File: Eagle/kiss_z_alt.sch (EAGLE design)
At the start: 7 parts, among them U1 LMX2326, U2 MAX2752, U3 RMK-3-93+

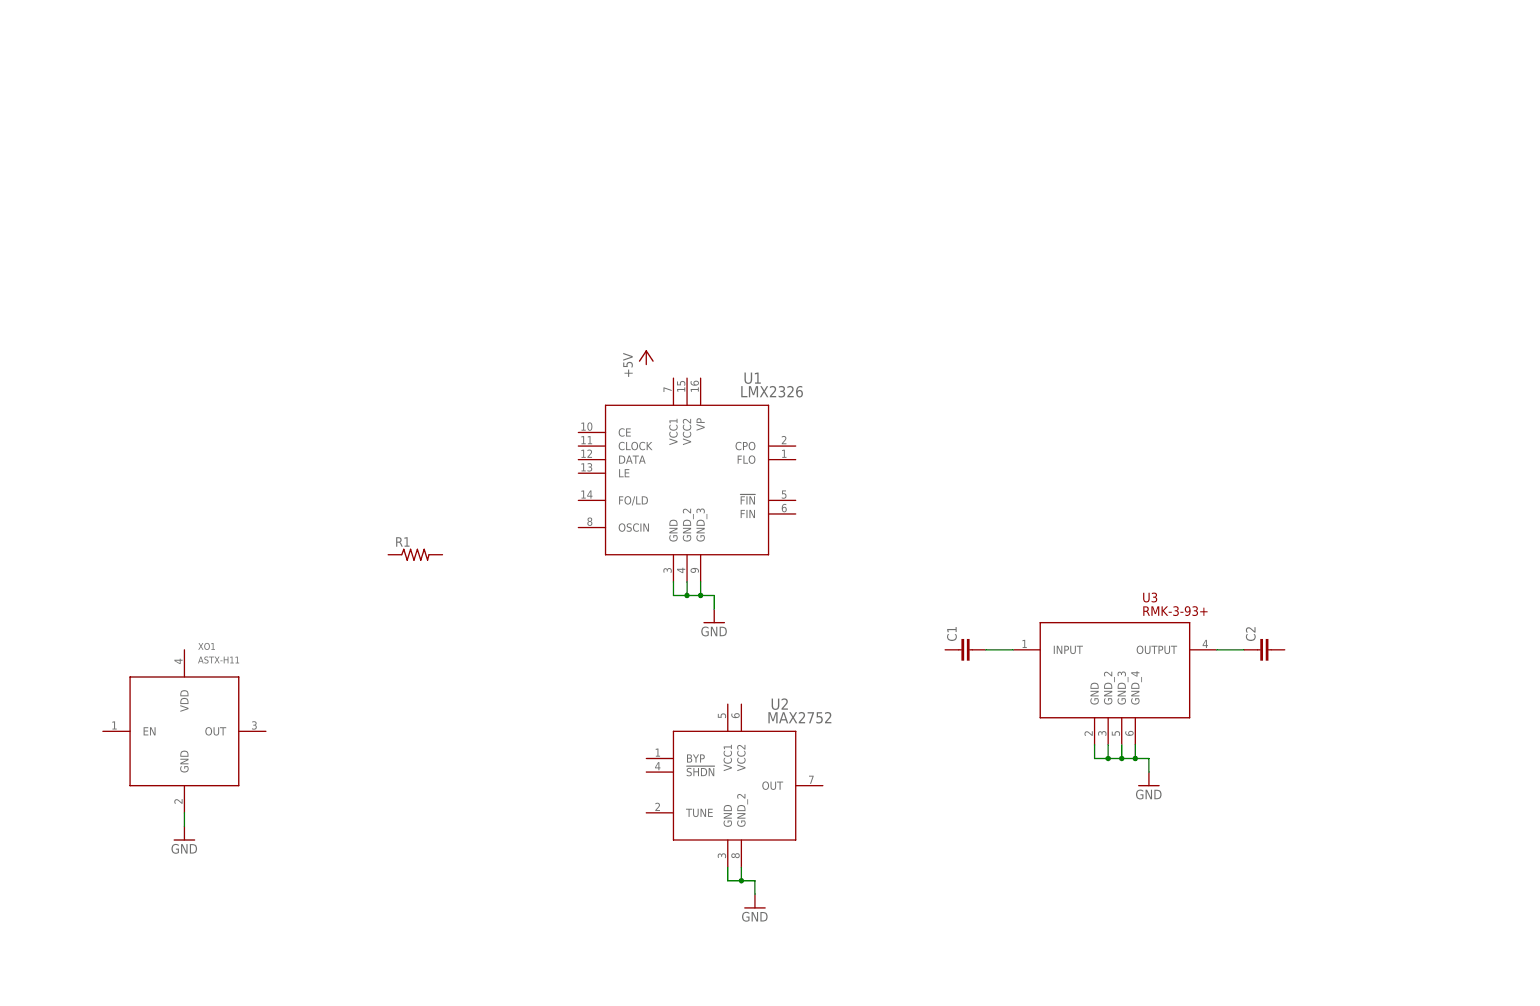
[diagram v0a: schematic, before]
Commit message: Making connections
made loop filter
started power connections
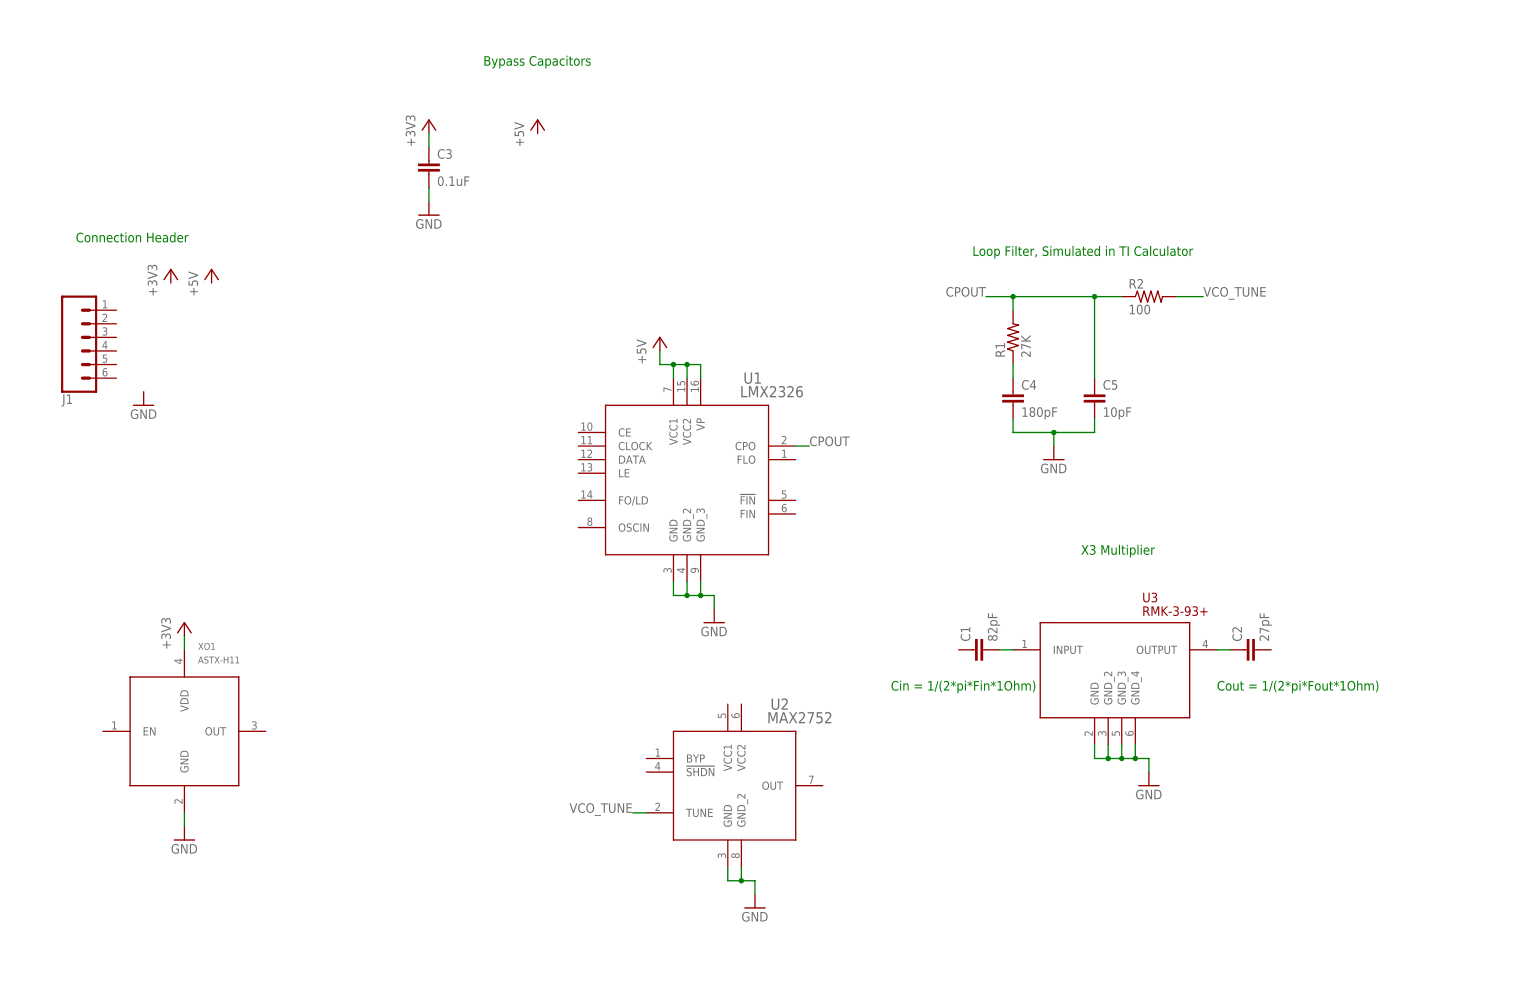
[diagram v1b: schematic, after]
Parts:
- added C3: 0.1uF, kiss_z:C0603
- added C4: 180pF, kiss_z:C0603
- added C5: 10pF, kiss_z:C0603
- added J1: (no value), SparkFun-Connectors:CONN_06SILK_FEMALE_PTH
- added R2: 100, kiss_z:R0603
- C1: value (none) -> 82pF
- C2: value (none) -> 27pF
- R1: value (none) -> 27K
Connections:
- new net +3V3: XO1.VDD
- new net +5V: U1.VCC1, U1.VCC2, U1.VP
- new net CPOUT: U1.CPO
- new net N$3: C4.1, R1.1
- new net N$4: U2.TUNE
- new net N$5: C5.1, R1.2, R2.1
- new net N$6: C3.1
- new net VCO_TUNE: R2.2
- net GND: now also C3.2, C4.2, C5.2
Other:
- note added: "Bypass Capacitors"
- note added: "Cin = 1/(2*pi*Fin*1Ohm)"
- note added: "Connection Header"
- note added: "Cout = 1/(2*pi*Fout*1Ohm)"
- note added: "Loop Filter, Simulated in TI Calculator"
- note added: "X3 Multiplier"
- moved on the sheet: C1, C2, R1

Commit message: more connections
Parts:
- added C6: NP, kiss_z:C0603
- added R3: NP, kiss_z:R0603
- C3: value 0.1uF -> 100pF
- C4: value 180pF -> 82pF
- C5: value 10pF -> 12pF
- R1: value 27K -> 56K
- R2: value 100 -> NP
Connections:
- removed net VCO_TUNE: R2.2
- new net FL_OUT: U1.FLO
- new net MULT_OUT: C2.2
- new net N$7: C6.2, R2.2, R3.1
- new net N$8: R3.2
- new net VCO_OUT: U2.OUT
- net +3V3: now also XO1.EN
- net GND: now also R2.1
- net N$5: now also C6.1; no longer R2.1
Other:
- note added: "VCO"
- moved on the sheet: R2
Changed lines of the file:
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@@
 <part name="XO1" library="kiss_z" deviceset="ASTX-H11" device=""/>
 <part name="U2" library="kiss_z" deviceset="MAX2752" device=""/>
-<part name="R1" library="kiss_z" deviceset="R0603" device="" value="27K"/>
+<part name="R1" library="kiss_z" deviceset="R0603" device="" value="56K"/>
 <part name="U3" library="kiss_z" deviceset="RMK-3-93+" device=""/>
 <part name="C1" library="kiss_z" deviceset="C0603" device="" value="82pF"/>
@@
 <part name="GND4" library="supply1" library_urn="urn:adsk.eagle:library:371" deviceset="GND" device=""/>
 <part name="+3V1" library="supply1" library_urn="urn:adsk.eagle:library:371" deviceset="+3V3" device=""/>
-<part name="C3" library="kiss_z" deviceset="C0603" device="" value="0.1uF"/>
+<part name="C3" library="kiss_z" deviceset="C0603" device="" value="100pF"/>
 <part name="GND5" library="supply1" library_urn="urn:adsk.eagle:library:371" deviceset="GND" device=""/>
-<part name="C4" library="kiss_z" deviceset="C0603" device="" value="180pF"/>
-<part name="C5" library="kiss_z" deviceset="C0603" device="" value="10pF"/>
+<part name="C4" library="kiss_z" deviceset="C0603" device="" value="82pF"/>
+<part name="C5" library="kiss_z" deviceset="C0603" device="" value="12pF"/>
 <part name="GND6" library="supply1" library_urn="urn:adsk.eagle:library:371" deviceset="GND" device=""/>
-<part name="R2" library="kiss_z" deviceset="R0603" device="" value="100"/>
 <part name="J1" library="SparkFun-Connectors" library_urn="urn:adsk.eagle:library:513" deviceset="CONN_06" device="SILK_FEMALE_PTH" package3d_urn="urn:adsk.eagle:package:38009/1"/>
 <part name="+3V2" library="supply1" library_urn="urn:adsk.eagle:library:371" deviceset="+3V3" device=""/>
@@
 <part name="+3V3" library="supply1" library_urn="urn:adsk.eagle:library:371" deviceset="+3V3" device=""/>
 <part name="P+3" library="supply1" library_urn="urn:adsk.eagle:library:371" deviceset="+5V" device=""/>
+<part name="R2" library="kiss_z" deviceset="R0603" device="" value="NP"/>
+<part name="R3" library="kiss_z" deviceset="R0603" device="" value="NP"/>
+<part name="C6" library="kiss_z" deviceset="C0603" device="" value="NP"/>
 </parts>
 <sheets>
@@
 <text x="165.1" y="53.34" size="1.778" layer="91">Cin = 1/(2*pi*Fin*1Ohm)</text>
 <text x="226.06" y="53.34" size="1.778" layer="91">Cout = 1/(2*pi*Fout*1Ohm)</text>
-<text x="180.34" y="134.62" size="1.778" layer="91">Loop Filter, Simulated in TI Calculator</text>
-<text x="200.66" y="78.74" size="1.778" layer="91">X3 Multiplier</text>
+<text x="193.04" y="134.62" size="1.778" layer="91">Loop Filter, Simulated in TI Calculator</text>
+<text x="200.66" y="73.66" size="1.778" layer="91">X3 Multiplier</text>
 <text x="12.7" y="137.16" size="1.778" layer="91">Connection Header</text>
 <text x="88.9" y="170.18" size="1.778" layer="91">Bypass Capacitors</text>
+<text x="76.2" y="162.56" size="1.778" layer="91">VCO</text>
 </plain>
 <instances>
@@
 <instance part="GND3" gate="1" x="132.08" y="66.04"/>
 <instance part="GND4" gate="1" x="33.02" y="25.4"/>
-<instance part="+3V1" gate="G$1" x="33.02" y="66.04"/>
+<instance part="+3V1" gate="G$1" x="12.7" y="68.58"/>
 <instance part="C3" gate="G$1" x="78.74" y="152.4"/>
 <instance part="GND5" gate="1" x="78.74" y="142.24"/>
 <instance part="C4" gate="G$1" x="187.96" y="109.22"/>
 <instance part="C5" gate="G$1" x="203.2" y="109.22"/>
-<instance part="GND6" gate="1" x="195.58" y="96.52"/>
-<instance part="R2" gate="G$1" x="213.36" y="127"/>
+<instance part="GND6" gate="1" x="223.52" y="96.52"/>
 <instance part="J1" gate="G$1" x="15.24" y="119.38" rot="MR180"/>
 <instance part="+3V2" gate="G$1" x="30.48" y="132.08"/>
@@
 <instance part="+3V3" gate="G$1" x="78.74" y="160.02"/>
 <instance part="P+3" gate="1" x="99.06" y="160.02"/>
+<instance part="R2" gate="G$1" x="220.98" y="114.3" rot="R90"/>
+<instance part="R3" gate="G$1" x="231.14" y="127"/>
+<instance part="C6" gate="G$1" x="210.82" y="127" rot="R90"/>
 </instances>
 <busses>
@@
 <pinref part="C5" gate="G$1" pin="2"/>
 <wire x1="203.2" y1="104.14" x2="203.2" y2="101.6" width="0.1524" layer="91"/>
-<wire x1="203.2" y1="101.6" x2="195.58" y2="101.6" width="0.1524" layer="91"/>
 <pinref part="C4" gate="G$1" pin="2"/>
-<wire x1="195.58" y1="101.6" x2="187.96" y2="101.6" width="0.1524" layer="91"/>
+<wire x1="203.2" y1="101.6" x2="187.96" y2="101.6" width="0.1524" layer="91"/>
 <wire x1="187.96" y1="101.6" x2="187.96" y2="104.14" width="0.1524" layer="91"/>
+<pinref part="R2" gate="G$1" pin="1"/>
+<wire x1="220.98" y1="109.22" x2="220.98" y2="101.6" width="0.1524" layer="91"/>
+<wire x1="220.98" y1="101.6" x2="203.2" y2="101.6" width="0.1524" layer="91"/>
+<junction x="203.2" y="101.6"/>
 <pinref part="GND6" gate="1" pin="GND"/>
-<wire x1="195.58" y1="101.6" x2="195.58" y2="99.06" width="0.1524" layer="91"/>
-<junction x="195.58" y="101.6"/>
-</segment>
-</net>
-<net name="+3V3" class="0">
-<segment>
-<pinref part="XO1" gate="A" pin="VDD"/>
-<wire x1="33.02" y1="63.5" x2="33.02" y2="60.96" width="0.1524" layer="91"/>
-<pinref part="+3V1" gate="G$1" pin="+3V3"/>
+<wire x1="220.98" y1="101.6" x2="223.52" y2="101.6" width="0.1524" layer="91"/>
+<wire x1="223.52" y1="101.6" x2="223.52" y2="99.06" width="0.1524" layer="91"/>
+<junction x="220.98" y="101.6"/>
 </segment>
 </net>
@@
 <wire x1="187.96" y1="127" x2="182.88" y2="127" width="0.1524" layer="91"/>
 <junction x="187.96" y="127"/>
+<pinref part="C6" gate="G$1" pin="1"/>
 <wire x1="203.2" y1="127" x2="208.28" y2="127" width="0.1524" layer="91"/>
 <junction x="203.2" y="127"/>
-<pinref part="R2" gate="G$1" pin="1"/>
 </segment>
 </net>
@@
 <segment>
 <label x="182.88" y="127" size="1.778" layer="95" rot="MR0"/>
-</segment>
-</net>
-<net name="VCO_TUNE" class="0">
-<segment>
-<pinref part="R2" gate="G$1" pin="2"/>
-<wire x1="218.44" y1="127" x2="223.52" y2="127" width="0.1524" layer="91"/>
-<label x="223.52" y="127" size="1.778" layer="95"/>
 </segment>
 <segment>
@@
 </segment>
 </net>
+<net name="VCO_OUT" class="0">
+<segment>
+<pinref part="U2" gate="A" pin="OUT"/>
+<wire x1="152.4" y1="35.56" x2="154.94" y2="35.56" width="0.1524" layer="91"/>
+<label x="154.94" y="35.56" size="1.778" layer="95"/>
+</segment>
+<segment>
+<wire x1="175.26" y1="60.96" x2="177.8" y2="60.96" width="0.1524" layer="91"/>
+<label x="175.26" y="60.96" size="1.778" layer="95" rot="MR0"/>
+</segment>
+</net>
+<net name="MULT_OUT" class="0">
+<segment>
+<pinref part="C2" gate="G$1" pin="2"/>
+<wire x1="236.22" y1="60.96" x2="238.76" y2="60.96" width="0.1524" layer="91"/>
+<label x="238.76" y="60.96" size="1.778" layer="95"/>
+</segment>
+</net>
+<net name="FL_OUT" class="0">
+<segment>
+<pinref part="U1" gate="A" pin="FLO"/>
+<wire x1="147.32" y1="96.52" x2="149.86" y2="96.52" width="0.1524" layer="91"/>
+<label x="149.86" y="96.52" size="1.778" layer="95"/>
+</segment>
+<segment>
+<label x="241.3" y="127" size="1.778" layer="95"/>
+</segment>
+</net>
+<net name="N$7" class="0">
+<segment>
+<pinref part="C6" gate="G$1" pin="2"/>
+<pinref part="R3" gate="G$1" pin="1"/>
+<wire x1="215.9" y1="127" x2="220.98" y2="127" width="0.1524" layer="91"/>
+<pinref part="R2" gate="G$1" pin="2"/>
+<wire x1="220.98" y1="127" x2="226.06" y2="127" width="0.1524" layer="91"/>
+<wire x1="220.98" y1="127" x2="220.98" y2="119.38" width="0.1524" layer="91"/>
+<junction x="220.98" y="127"/>
+</segment>
+</net>
+<net name="N$8" class="0">
+<segment>
+<pinref part="R3" gate="G$1" pin="2"/>
+<wire x1="236.22" y1="127" x2="241.3" y2="127" width="0.1524" layer="91"/>
+</segment>
+</net>
+<net name="+3V3" class="0">
+<segment>
+<pinref part="+3V1" gate="G$1" pin="+3V3"/>
+<wire x1="12.7" y1="66.04" x2="12.7" y2="63.5" width="0.1524" layer="91"/>
+<pinref part="XO1" gate="A" pin="EN"/>
+<wire x1="17.78" y1="45.72" x2="15.24" y2="45.72" width="0.1524" layer="91"/>
+<wire x1="15.24" y1="45.72" x2="15.24" y2="63.5" width="0.1524" layer="91"/>
+<wire x1="15.24" y1="63.5" x2="33.02" y2="63.5" width="0.1524" layer="91"/>
+<pinref part="XO1" gate="A" pin="VDD"/>
+<wire x1="33.02" y1="63.5" x2="33.02" y2="60.96" width="0.1524" layer="91"/>
+<wire x1="12.7" y1="63.5" x2="15.24" y2="63.5" width="0.1524" layer="91"/>
+<junction x="15.24" y="63.5"/>
+</segment>
+</net>

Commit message: more connections...
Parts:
- added C10, C7, C8: 100pF, kiss_z:C0603
- added C11, C9: 0.1uF, kiss_z:C0603
- added R4: 18, kiss_z:R0603
- added R5: 10, kiss_z:R0603
- added R6: 100k, kiss_z:R0603
- J1: device SparkFun-Connectors:CONN_06SILK_FEMALE_PTH -> SparkFun-Connectors:CONN_08"
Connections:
- net +5V renamed N$11
- new net N$10: C7.1, U1.OSCIN
- new net N$14: C10.2, C11.2
- new net N$9: XO1.OUT
- new net PLL_CE: U1.CE
- new net PLL_CLK: U1.CLOCK
- new net PLL_LE: U1.LE
- new net PLL_MOSI: U1.DATA
- new net PLL_MUX: U1.FO/LD
- new net PLL_VCC: R4.2
- new net TCXO_EN: J1.2, R6.2, XO1.EN
- new net TCXO_OUT: C7.2
- new net VCO_VCC: R5.2, U2.VCC1, U2.VCC2
- net +3V3: now also C10.1, C11.1, C8.1, C9.1, J1.1, R4.1, R5.1; no longer XO1.EN
- net GND: now also C8.2, C9.2, J1.8, R6.1
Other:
- note added: "PLL"
- note added: "TCXO"
- moved on the sheet: C3

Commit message: started running erc
still needs power divider
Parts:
- removed R2: NP, kiss_z:R0603
- added C12: 0.1uF, kiss_z:C0603
- C6: value NP -> 100pF
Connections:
- removed net N$11: U1.VCC1, U1.VCC2, U1.VP
- removed net N$14: C10.2, C11.2
- removed net N$4: U2.TUNE
- removed net N$6: C3.1
- removed net N$8: R3.2
- removed net N$9: XO1.OUT
- removed net TCXO_EN: J1.2, R6.2, XO1.EN
- new net CP_OUT: C5.1, R1.2, U2.TUNE
- new net OSC_EN: J1.2, R6.2, U2.!SHDN, XO1.EN
- net +3V3: now also C3.1
- net FL_OUT: now also R3.2
- net GND: now also C10.2, C11.2, C12.2, C6.2; no longer R2.1
- net N$3: now also R3.1
- net N$5: now also U1.!FIN; no longer C5.1, R1.2
- net N$7: now also C12.1, U2.BYP; no longer C6.2, R2.2, R3.1
- net PLL_MUX: now also J1.7
- net PLL_VCC: now also U1.VCC1, U1.VCC2, U1.VP
- net TCXO_OUT: now also XO1.OUT
- net VCO_OUT: now also C1.1
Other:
- note added: "Loop Filter"
- note added: "Phase-Locked Loop"
- note added: "Temperature-Compensated Crystal Oscillaor"
- note added: "Voltage-Controlled Oscillator"
- note added: "X3 Frequency Multiplier"
- note removed: "Loop Filter, Simulated in TI Calculator"
- note removed: "X3 Multiplier"
- moved on the sheet: C1, C2, C4, C5, C6, C7, R1, R3, R6, U1, U2, U3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
